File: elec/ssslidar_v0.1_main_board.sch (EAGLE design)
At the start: 6 parts

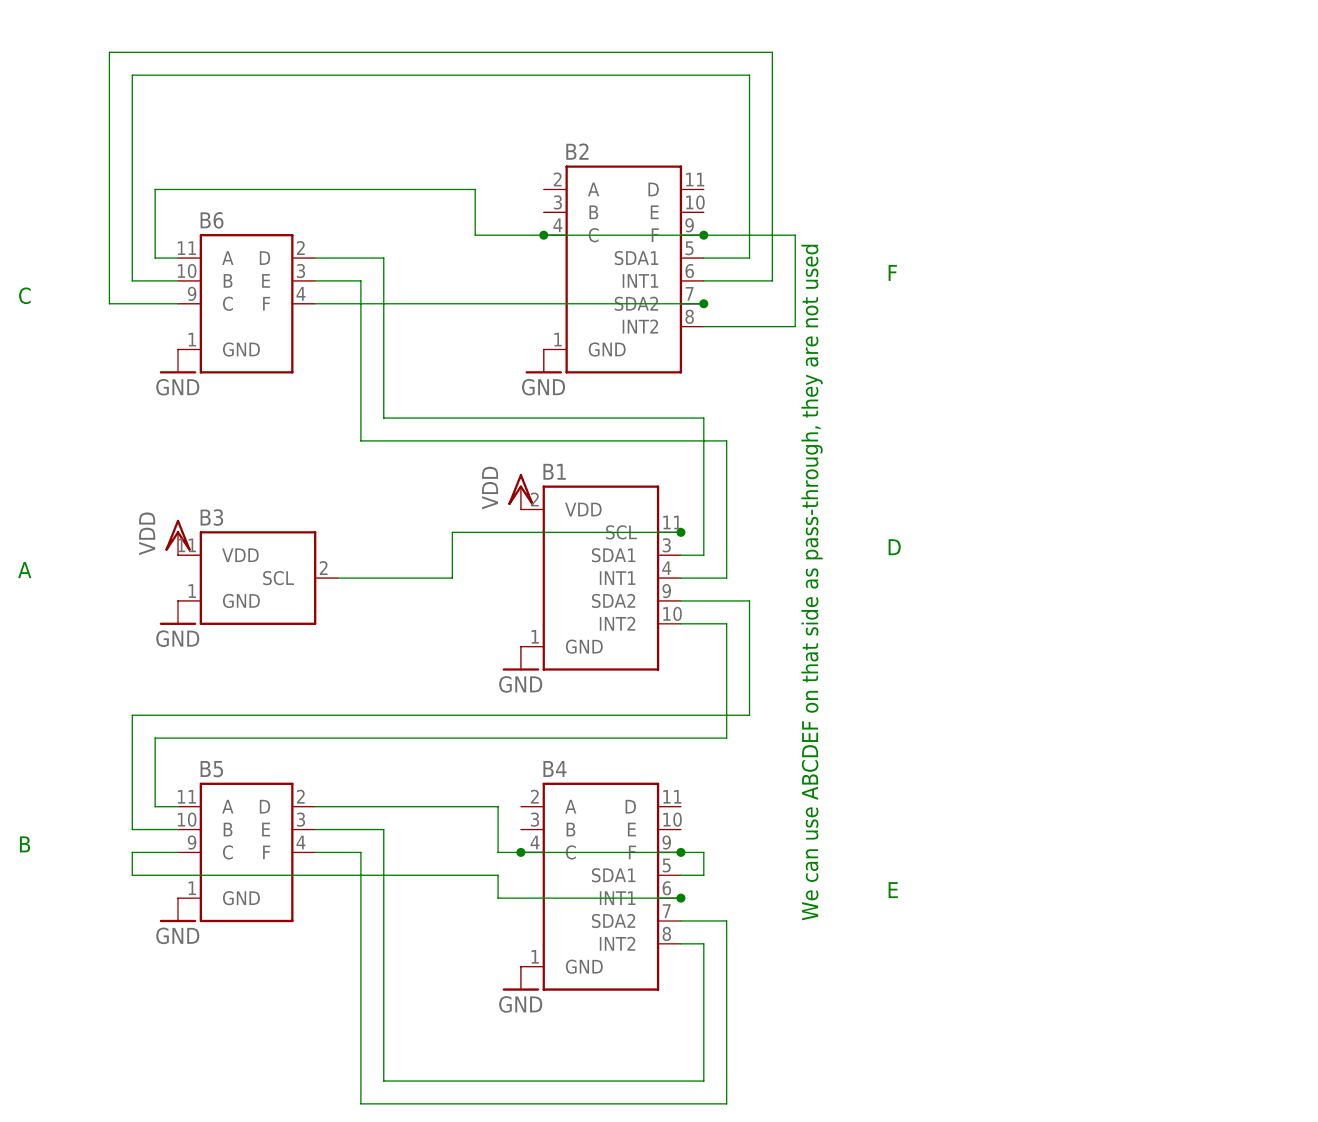
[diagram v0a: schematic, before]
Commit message: Added main board (wip)
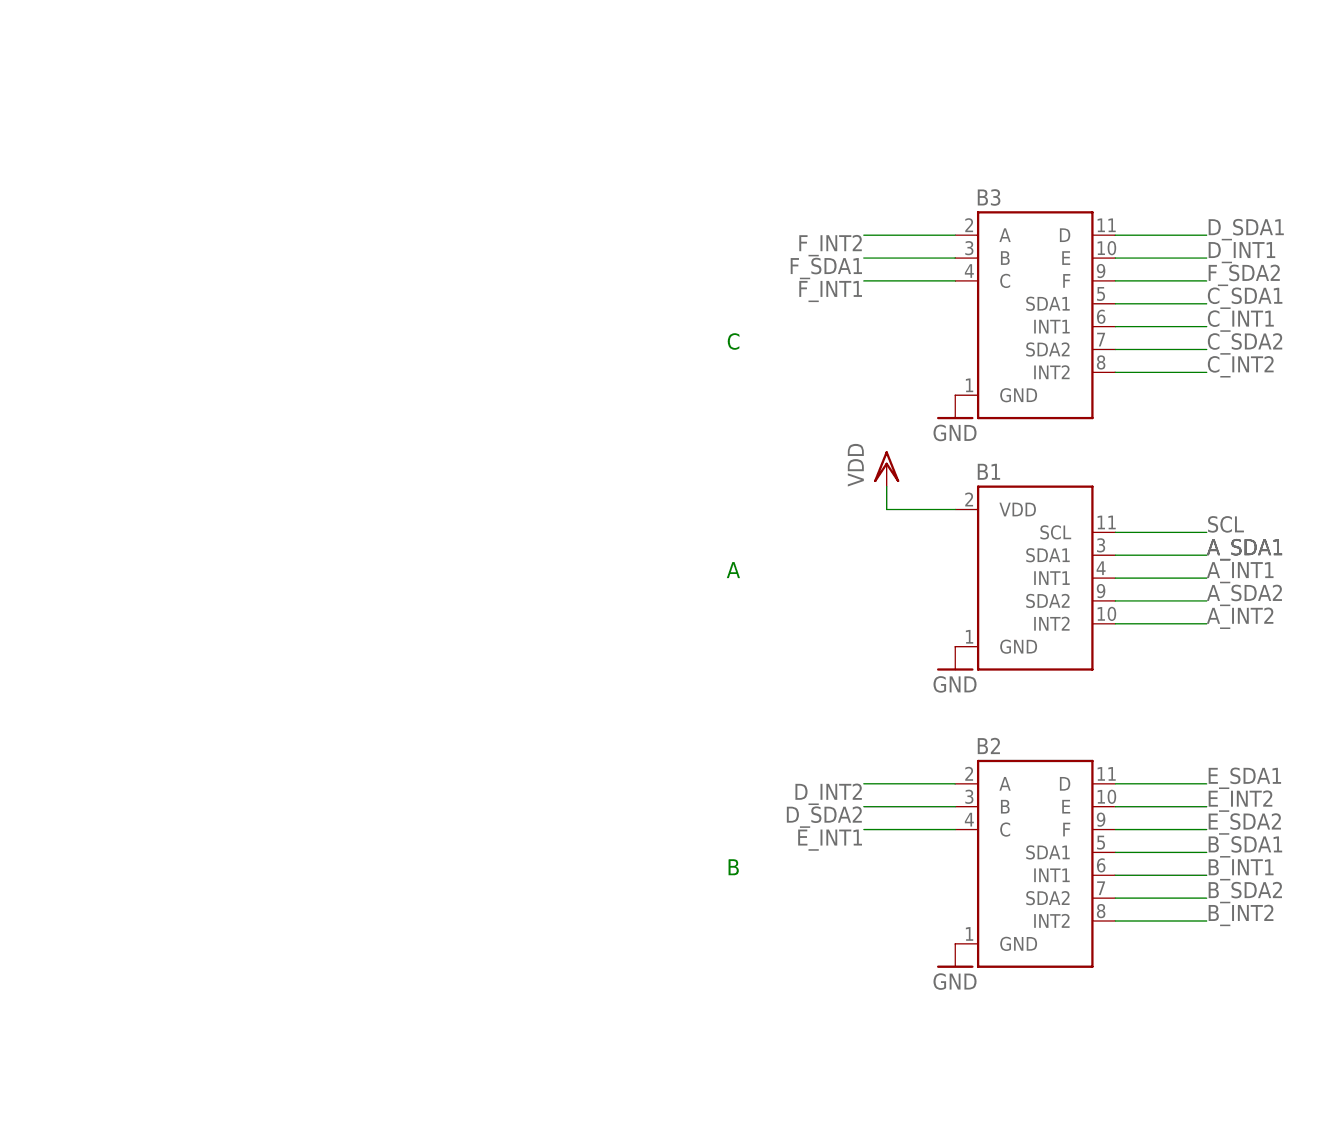
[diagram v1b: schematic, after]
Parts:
- removed B4: (no value), ssslidar:BLADE_SIG_BOTTOM
- removed B5, B6: (no value), ssslidar:BLADE_SIG_TOP
- B3: device ssslidar:BLADE_PWR_TOP -> ssslidar:BLADE_SIG_BOTTOM
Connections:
- removed net N$1: B1.SCL, B3.SCL
- removed net N$10: B4.C, B4.F, B4.SDA1, B5.D
- removed net N$11: B4.INT1, B5.C
- removed net N$12: B1.SDA2, B5.B
- removed net N$13: B1.INT2, B5.A
- removed net N$14: B1.SDA1, B6.D
- removed net N$2: B2.C, B2.F, B2.INT2, B6.A
- removed net N$21: B4.SDA2, B5.F
- removed net N$3: B2.SDA1, B6.B
- removed net N$4: B2.INT1, B6.C
- removed net N$6: B1.INT1, B6.E
- removed net N$7: B2.SDA2, B6.F
- removed net N$8: B4.INT2, B5.E
- new net A_INT1: B1.INT1
- new net A_INT2: B1.INT2
- new net A_SDA1: B1.SDA1
- new net A_SDA2: B1.SDA2
- new net B_INT1: B2.INT1
- new net B_INT2: B2.INT2
- new net B_SDA1: B2.SDA1
- new net B_SDA2: B2.SDA2
- new net C_INT1: B3.INT1
- new net C_INT2: B3.INT2
- new net C_SDA1: B3.SDA1
- new net C_SDA2: B3.SDA2
- new net D_INT1: B3.E
- new net D_INT2: B2.A
- new net D_SDA1: B3.D
- new net D_SDA2: B2.B
- new net E_INT1: B2.C
- new net E_INT2: B2.E
- new net E_SDA1: B2.D
- new net E_SDA2: B2.F
- new net F_INT1: B3.C
- new net F_INT2: B3.A
- new net F_SDA1: B3.B
- new net F_SDA2: B3.F
- new net SCL: B1.SCL
- net GND: no longer B4.GND, B5.GND, B6.GND
- net VDD: no longer B3.VDD
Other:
- note removed: "D"
- note removed: "E"
- note removed: "F"
- note removed: "We can use ABCDEF on that side as pass-through, they are not used"
- moved on the sheet: B1, B2

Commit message: Working on main board Made blades longer to avoid too much occlusion from the main PCB (but we will still need to put the whole thing on a mast).
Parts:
- added C1: 10uF, Xevelabs:C0805
- added C2: 100nF, Xevelabs:C0402
- added C3, C4: (no value), Xevelabs:C1206
- added JP1: FTDI_DEVICE, SparkFun-Connectors:FTDI_DEVICE
- added R1, R2, R3: (no value), Xevelabs:R0402
- added U$1: 74HC4067DB,118, SparkFun-AnalogIC:MUX-74HC4067SMD
- added U1: VL53L0X, VL53L0X:VL53L0X
- added U2: TLV1117LV28DCYR, OPL:CJ1117-3.3-1310190P1
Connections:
- new net !SDA_MUX_EN: U$1.EN
- new net +5V: C3.1, U2.IN
- new net G_INT1: U1.GPIO1
- new net G_SDA1: R3.1, U$1.CHAN12, U1.SDA
- new net SDA: R1.1, U$1.COM
- new net SDA_ADDR0: U$1.S0
- new net SDA_ADDR1: U$1.S1
- new net SDA_ADDR2: U$1.S2
- new net SDA_ADDR3: U$1.S3
- net A_SDA1: now also U$1.CHAN0
- net A_SDA2: now also U$1.CHAN1
- net B_SDA1: now also U$1.CHAN2
- net B_SDA2: now also U$1.CHAN3
- net C_SDA1: now also U$1.CHAN4
- net C_SDA2: now also U$1.CHAN5
- net D_SDA1: now also U$1.CHAN6
- net D_SDA2: now also U$1.CHAN7
- net E_SDA1: now also U$1.CHAN8
- net E_SDA2: now also U$1.CHAN9
- net F_SDA1: now also U$1.CHAN10
- net F_SDA2: now also U$1.CHAN11
- net GND: now also C1.2, C2.2, C3.2, C4.2, JP1.CTS, U$1.GND, U1.AVSSVCSEL, U1.GND, U2.GND
- net SCL: now also R2.1, U1.SCL
- net VDD: now also C1.1, C2.1, C4.1, R1.2, R2.2, R3.2, U$1.VCC, U1.AVDD, U1.AVDDVCSEL, U1.XSHUT, U2.OUT
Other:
- note added: "2.8V >500ma"
- note added: "TODO SWD"

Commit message: Updated blades (ready for release). Double power rail for sensors.
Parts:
- removed R1: (no value), Xevelabs:R0402
- removed U2: TLV1117LV28DCYR, OPL:CJ1117-3.3-1310190P1
- added C10, C9: 6pF, Xevelabs:C0201
- added C12, C8: 4.7uF 10V, Xevelabs:C0603
- added C13, C14: 100nF, Xevelabs:C0201
- added C16: 470pF, Xevelabs:C0201
- added C5, C6: (no value), Xevelabs:C1206
- added C7: 10uF 25V, Xevelabs:C0805
- added JP3: DXL_EXT, SparkFun-Connectors:M061.27MM
- added LED1: yellow, Xevelabs:LED0603_L
- added P1, P10, P11, P12, P14, P15, P2, P3, P4, P5, P6, P7: PIN_SMD_0.8X1.6, Xevelabs:PIN_SMD_0.8X1.6
- added Q1: XRCGB24M000F3M00R0 (24MHz), Xevelabs:CRYSTAL_W/BODY-2.0X1.6
- added R6: 470, Xevelabs:R0201
- added U$2: 74HC4067DB,118, SparkFun-AnalogIC:MUX-74HC4067SMD
- added U3: MIC5235-5.0YM5, SparkFun-PowerIC:V_REG_MIC5235
- added U4: STM32F301K6U6, stm32F301:STM32F301K6U6
- added U7: MIC5205-3.3YM5, OPL:MIC5205-3.3YM5
- R2, R3: value (none) -> 2k
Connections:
- removed net !SDA_MUX_EN: U$1.EN
- removed net SDA_ADDR0: U$1.S0
- removed net SDA_ADDR1: U$1.S1
- removed net SDA_ADDR2: U$1.S2
- removed net SDA_ADDR3: U$1.S3
- new net !MUX_EN: U$1.EN, U$2.EN
- new net +12V: C7.1, U3.EN, U3.IN
- new net +3V3: C12.1, C13.1, C14.1, LED1.A, P10.1, U4.VDD, U4.VDDA/VREF+, U7.VOUT
- new net COM_RST: P14.1, U4.NRST
- new net COM_RX: U4.PA9
- new net COM_TX: U4.PA10
- new net DBG_GPIO1: P3.1, U4.PB4
- new net DBG_GPIO2: P7.1, U4.PA1
- new net DBG_GPIO3: P6.1, U4.PA0
- new net DBG_RX: P5.1, U4.PA15
- new net DBG_TX: P4.1, U4.PB3
- new net DXL<MCU: JP3.2
- new net DXL>MCU: JP3.1
- new net IMU_SCL: U4.PA8
- new net IMU_SDA: U4.PB5
- new net INT: U$2.COM
- new net LED: R6.2, U4.PB7
- new net MPU_INT: U4.PA11
- new net MUX_ADDR0: U$1.S0, U$2.S0
- new net MUX_ADDR1: U$1.S1, U$2.S1
- new net MUX_ADDR2: U$1.S2, U$2.S2
- new net MUX_ADDR3: U$1.S3, U$2.S3
- new net N$1: C10.1, Q1.P$1, U4.PF0-OSC_IN
- new net N$10: JP3.4
- new net N$11: JP3.6
- new net N$2: C9.1, Q1.P$2, U4.PF1-OSC_OUT
- new net N$4: LED1.C, R6.1
- new net N$7: C16.1, U7.BYP
- new net N$9: JP3.3
- new net RX_EN: U4.PA12
- new net SWCLK: P11.1, U4.PA14
- new net SWDIO: P12.1, U4.PA13
- new net VEE: B1.VDD_PASS, C1.1, C2.1, C6.1, R3.2, U1.AVDD, U1.AVDDVCSEL
- net +5V: now also C5.1, C8.1, U3.OUT, U7.EN, U7.VIN; no longer U2.IN
- net A_INT1: now also U$2.CHAN0
- net A_INT2: now also U$2.CHAN1
- net B_INT1: now also U$2.CHAN2
- net B_INT2: now also U$2.CHAN3
- net C_INT1: now also U$2.CHAN4
- net C_INT2: now also U$2.CHAN5
- net D_INT1: now also U$2.CHAN6
- net D_INT2: now also U$2.CHAN7
- net E_INT1: now also U$2.CHAN8
- net E_INT2: now also U$2.CHAN9
- net F_INT1: now also U$2.CHAN10
- net F_INT2: now also U$2.CHAN11
- net GND: now also C10.2, C12.2, C13.2, C14.2, C16.2, C5.2, C6.2, C7.2, C8.2, C9.2, JP3.5, P1.1, P15.1, P2.1, Q1.GND, U$2.GND, U3.GND, U4.BOOT0, U4.VSS, U4.VSSA/VREF-, U7.GND; no longer U2.GND
- net G_INT1: now also U$2.CHAN12
- net SDA: no longer R1.1
- net VDD: now also U$2.VCC; no longer C1.1, C2.1, R1.2, R3.2, U1.AVDD, U1.AVDDVCSEL, U2.OUT
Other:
- note added: "(C) 2016 - Nicolas Saugnier - Xevelabs.com"
- note added: "2.8V >250mA each"
- note added: "200mA@5V from 6-18V 150mA@3V3 from 5V"
- note added: "ALT (pinout to be verified): MCP1804T-5002I/OT XC6701B502MR LM3490IM5-5.0/NOPB"
- note added: "ALT: XRCGB32M000F0Z00R0 (32MHz)"
- note added: "Connectors"
- note added: "LED"
- note added: "MCU"
- note added: "NC"
- note added: "Power"
- note added: "Sensors"
- note added: "TODO 12"
- note added: "TODO 3V3"
- note added: "TODO 5"
- note removed: "2.8V >500ma"
- note removed: "TODO SWD"
- moved on the sheet: C1, C2, C3, C4, R2, R3, U$1, U1

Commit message: Main board outline and schematics nearly ready
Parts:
- removed C12, C8: 4.7uF 10V, Xevelabs:C0603
- removed C16: 470pF, Xevelabs:C0201
- removed P1: PIN_SMD_0.8X1.6, Xevelabs:PIN_SMD_0.8X1.6
- removed U3: MIC5235-5.0YM5, SparkFun-PowerIC:V_REG_MIC5235
- removed U7: MIC5205-3.3YM5, OPL:MIC5205-3.3YM5
- added C11: 22uF, Xevelabs:C1206_L
- added D1, D2: (no value), OPL:D-SOD-123
- added IC1, IC2: MIC5504-2.8YM5, v-reg-micrel:MIC5219XX
- added JP2: EXT_PWR, pinhead:PINHD-1X2
- added L2: VLS2012ET-2R2M, Xevelabs:L2016M
- added P8: PIN_SMD_0.8X1.6, Xevelabs:PIN_SMD_0.8X1.6
- added U2: TPS62173DSG, Xevelabs:IC_TPS62160DSG_L
- C7: value 10uF 25V -> 22uF@16V; device Xevelabs:C0805 -> Xevelabs:C1206_L
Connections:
- removed net +3V3: C12.1, C13.1, C14.1, LED1.A, P10.1, U4.VDD, U4.VDDA/VREF+, U7.VOUT
- removed net COM_RX: U4.PA9
- removed net COM_TX: U4.PA10
- removed net IMU_SCL: U4.PA8
- removed net IMU_SDA: U4.PB5
- removed net MPU_INT: U4.PA11
- removed net N$10: JP3.4
- removed net N$11: JP3.6
- removed net N$9: JP3.3
- removed net RX_EN: U4.PA12
- new net DBG_GPIO4: P8.1
- new net N$3: L2.1, U2.SW
- new net N$5: C7.1, D1.-, U2.EN, U2.VIN
- new net RXD: JP1.RXI
- new net TXD: JP1.TXO
- net +12V: now also D1.+, JP2.1, JP3.6; no longer C7.1, U3.EN, U3.IN
- net +5V: now also D2.+, JP1.VCC; no longer C3.1, C5.1, C8.1, U3.OUT, U7.EN, U7.VIN
- net DBG_GPIO1: no longer U4.PB4
- net DBG_GPIO2: no longer U4.PA1
- net DBG_GPIO3: no longer U4.PA0
- net DBG_RX: no longer U4.PA15
- net DBG_TX: no longer U4.PB3
- net GND: now also C11.2, IC1.GND, IC2.GND, JP1.GND, JP2.2, U2.AGND, U2.FB, U2.PGND; no longer C12.2, C16.2, C8.2, P1.1, U3.GND, U7.GND
- net N$7: now also C11.1, C3.1, C5.1, D2.-, IC1.EN, IC1.IN, IC2.EN, IC2.IN, L2.2, U2.VOS; no longer C16.1, U7.BYP
- net VDD: now also C13.1, C14.1, IC2.OUT, LED1.A, P10.1, U4.VDD, U4.VDDA/VREF+
- net VEE: now also IC1.OUT
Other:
- note added: "2.8V 300mA each"
- note added: "TODO DTR?"
- note removed: "2.8V >250mA each"
- note removed: "200mA@5V from 6-18V 150mA@3V3 from 5V"
- note removed: "ALT (pinout to be verified): MCP1804T-5002I/OT XC6701B502MR LM3490IM5-5.0/NOPB"
- note removed: "TODO 12"
- note removed: "TODO 3V3"
- note removed: "TODO 5"
- moved on the sheet: B1, B2, B3, C1, C10, C13, C14, C2, C3, C4, C5, C6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

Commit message: Added leds, finished sch
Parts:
- removed C1: 10uF, Xevelabs:C0805
- removed C5: (no value), Xevelabs:C1206
- removed LED1: yellow, Xevelabs:LED0603_L
- removed R6: 470, Xevelabs:R0201
- added C8: 100nF, Xevelabs:C0402
- added L1: Ferrite 10R BLM18BA100SN1D, Xevelabs:L0603
- added LED10, LED11, LED12, LED13, LED14, LED3, LED4, LED5, LED6, LED7, LED8, LED9: yellow, Xevelabs:LED0603_L
- added LED2: Blue, Xevelabs:LED0603_L
- added P1, P13, P16, P17, P18, P19, P20, P21, P22, P23, P24, P25, P26, P27, P28, P9: PIN_SMD_0.8X1.6, Xevelabs:PIN_SMD_0.8X1.6
- added R1: 470, Xevelabs:R0402
- added R4: 10k, Xevelabs:R0402
- added R5, R7, R8, R9: TBD, Xevelabs:R0402
- C10, C13, C14, C9: device Xevelabs:C0201 -> Xevelabs:C0402
- C3, C4, C6: value (none) -> 10uF; device Xevelabs:C1206 -> Xevelabs:C0805
- JP2: value EXT_PWR -> M021X02_NO_SILK; device pinhead:PINHD-1X2 -> SparkFun-Connectors:M021X02_NO_SILK
- P3, P6, P7, P8: value PIN_SMD_0.8X1.6 -> PIN_SMD_1X1; device Xevelabs:PIN_SMD_0.8X1.6 -> Xevelabs:PIN_SMD_1X1
- U2: device Xevelabs:IC_TPS62160DSG_L -> Xevelabs:IC_TPS62160DSG_N
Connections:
- removed net DBG_RX: P5.1
- removed net DBG_TX: P4.1
- removed net LED: R6.2, U4.PB7
- removed net N$4: LED1.C, R6.1
- new net DTR: C8.1, JP1.DTR
- new net LED1: R5.1, U4.PA0
- new net LED2: R7.1, U4.PA1
- new net LED3: R8.1, U4.PA2
- new net LED4: R9.1, U4.PA3
- new net N$10: LED10.C, LED3.C, LED4.A, LED5.C, LED6.A, LED9.A, R7.2
- new net N$11: LED11.A, LED12.C, LED5.A, LED6.C, LED7.A, LED8.C, R8.2
- new net N$12: LED10.A, LED13.C, LED14.A, LED7.C, LED8.A, LED9.C, R9.2
- new net N$6: C11.1, L1.1, L2.2, U2.VOS
- new net N$8: LED2.C, R1.1
- new net N$9: LED11.C, LED12.A, LED13.A, LED14.C, LED3.A, LED4.C, R5.2
- net !MUX_EN: now also U4.PB0
- net +12V: now also JP2.2; no longer JP2.1
- net COM_RST: now also C8.2, R4.2
- net DBG_GPIO1: now also U4.PA11
- net DBG_GPIO2: now also U4.PA12
- net DBG_GPIO3: now also U4.PA8
- net DBG_GPIO4: now also U4.PB5
- net DXL<MCU: now also U4.PB3
- net DXL>MCU: now also U4.PB4
- net GND: now also JP2.1, R1.2; no longer C1.2, C5.2, JP2.2
- net INT: now also U4.PA15
- net MUX_ADDR0: now also U4.PA4
- net MUX_ADDR1: now also U4.PA5
- net MUX_ADDR2: now also U4.PA6
- net MUX_ADDR3: now also U4.PA7
- net N$7: now also L1.2, LED2.A; no longer C11.1, C5.1, L2.2, U2.VOS
- net RXD: now also P5.1, U4.PB7
- net SCL: now also U4.PA9
- net SDA: now also U4.PA10
- net TXD: now also P4.1, U4.PB6
- net VDD: now also R4.1; no longer LED1.A
- net VEE: no longer C1.1
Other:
- note added: "TODO caps & passives"
- note added: "TODO shottky"
- note removed: "TODO DTR?"
- moved on the sheet: C13, C14, C3, C4, C6, IC1, IC2, JP1, JP2, JP3, L2, P10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

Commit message: Routing WIP
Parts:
- added K1: BUTTON-2P-REINFORCE-3100060P1, OPL:BUTTON-2P-REINFORCE-3100060P1
- B1: value (none) -> PWR
- B2, B3: value (none) -> SIG
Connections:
- new net N$4: K1.1
- net GND: now also K1.2, K1.S1, K1.S2
- net VDD: no longer U1.XSHUT
- net VEE: now also U1.XSHUT
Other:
- note added: "TODO connect button in place of a GPIO"
- moved on the sheet: B3, LED10, LED11, LED12, LED13, LED14, LED3, LED4, LED5, LED6, LED7, LED8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

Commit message: Routed blades
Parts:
- removed P1, P13, P16, P17, P18, P19, P20, P21, P22, P23, P24, P25, P26, P27, P28, P4, P5, P9: PIN_SMD_0.8X1.6, Xevelabs:PIN_SMD_0.8X1.6
- removed P8: PIN_SMD_1X1, Xevelabs:PIN_SMD_1X1
- added C1, C5: 100nF, Xevelabs:C0402
- LED10, LED11, LED12, LED13, LED14, LED3, LED4, LED5, LED6, LED7, LED8, LED9: device Xevelabs:LED0603_L -> Xevelabs:LED0402
- P10, P11, P12, P14, P15, P2: value PIN_SMD_0.8X1.6 -> PIN_SMD_1X1.6; device Xevelabs:PIN_SMD_0.8X1.6 -> Xevelabs:PIN_SMD_1X1.6
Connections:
- net N$7 renamed 5V_OUT
- removed net DBG_GPIO4: P8.1, U4.PB5
- net A_INT1: now also U$2.CHAN12; no longer U$2.CHAN0
- net A_INT2: now also U$2.CHAN11; no longer U$2.CHAN1
- net A_SDA1: now also U$1.CHAN12; no longer U$1.CHAN0
- net A_SDA2: now also U$1.CHAN11; no longer U$1.CHAN1
- net B_INT2: now also U$2.CHAN5; no longer U$2.CHAN3
- net B_SDA2: now also U$1.CHAN5; no longer U$1.CHAN3
- net C_INT1: now also U$2.CHAN7; no longer U$2.CHAN4
- net C_INT2: now also U$2.CHAN10; no longer U$2.CHAN5
- net C_SDA1: now also U$1.CHAN7; no longer U$1.CHAN4
- net C_SDA2: now also U$1.CHAN10; no longer U$1.CHAN5
- net DBG_GPIO1: no longer U4.PA11
- net DBG_GPIO2: no longer U4.PA12
- net DBG_GPIO3: no longer U4.PA8
- net D_INT1: now also U$2.CHAN8; no longer U$2.CHAN6
- net D_INT2: now also U$2.CHAN1; no longer U$2.CHAN7
- net D_SDA1: now also U$1.CHAN8; no longer U$1.CHAN6
- net D_SDA2: now also U$1.CHAN1; no longer U$1.CHAN7
- net E_INT1: now also U$2.CHAN3; no longer U$2.CHAN8
- net E_INT2: now also U$2.CHAN4; no longer U$2.CHAN9
- net E_SDA1: now also U$1.CHAN3; no longer U$1.CHAN8
- net E_SDA2: now also U$1.CHAN4; no longer U$1.CHAN9
- net F_INT1: now also U$2.CHAN6; no longer U$2.CHAN10
- net F_INT2: now also U$2.CHAN9; no longer U$2.CHAN11
- net F_SDA1: now also U$1.CHAN6; no longer U$1.CHAN10
- net F_SDA2: now also U$1.CHAN9; no longer U$1.CHAN11
- net GND: now also C1.2, C5.2
- net G_INT1: now also U$2.CHAN15; no longer U$2.CHAN12
- net G_SDA1: now also U$1.CHAN15; no longer U$1.CHAN12
- net RXD: no longer P5.1
- net TXD: no longer P4.1
- net VDD: now also C1.1, C5.1, R3.2
- net VEE: no longer R3.2
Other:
- moved on the sheet: K1, U$1, U$2

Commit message: LEDs routed. Mostly power left to route.
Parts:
- removed C8: 100nF, Xevelabs:C0402
- removed R4: 10k, Xevelabs:R0402
- LED10, LED11, LED12, LED13, LED14, LED3, LED4, LED5, LED6, LED7, LED8, LED9: device Xevelabs:LED0402 -> Xevelabs:LED0603
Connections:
- removed net DTR: C8.1, JP1.DTR
- net !MUX_EN: now also U4.PA7; no longer U4.PB0
- net A_INT1: now also B1.NC3
- net A_SDA2: now also B1.NC1, B1.NC2
- net COM_RST: no longer C8.2, R4.2
- net DBG_GPIO1: now also U4.PB5
- net DBG_GPIO2: now also U4.PA6
- net DBG_GPIO3: now also U4.PA5
- net LED1: now also U4.PA2; no longer U4.PA0
- net LED2: now also U4.PA3; no longer U4.PA1
- net LED3: now also U4.PA0; no longer U4.PA2
- net LED4: now also U4.PA1; no longer U4.PA3
- net MUX_ADDR0: now also U4.PA11; no longer U4.PA4
- net MUX_ADDR1: now also U4.PA12; no longer U4.PA5
- net MUX_ADDR2: now also U4.PB0; no longer U4.PA6
- net MUX_ADDR3: now also U4.PA8; no longer U4.PA7
- net N$4: now also U4.PA4
- net VDD: no longer R4.1
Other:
- moved on the sheet: K1
